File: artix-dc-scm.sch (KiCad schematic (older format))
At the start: 2 parts

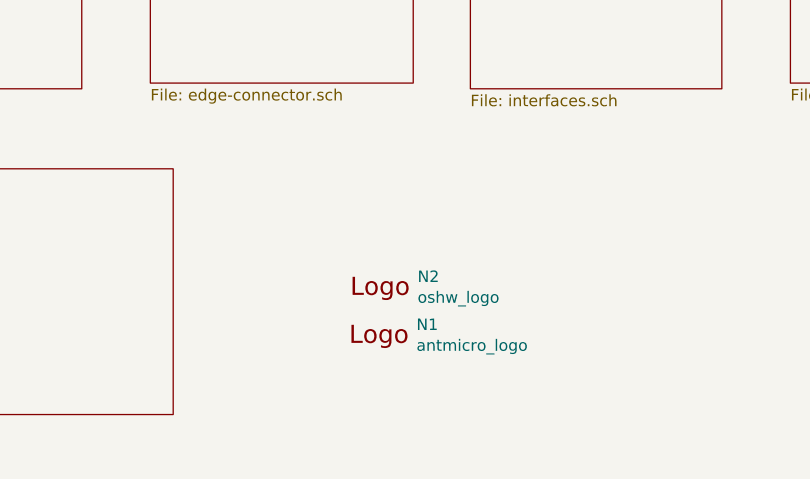
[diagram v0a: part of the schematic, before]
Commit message: Exposed copper and large mounting holes
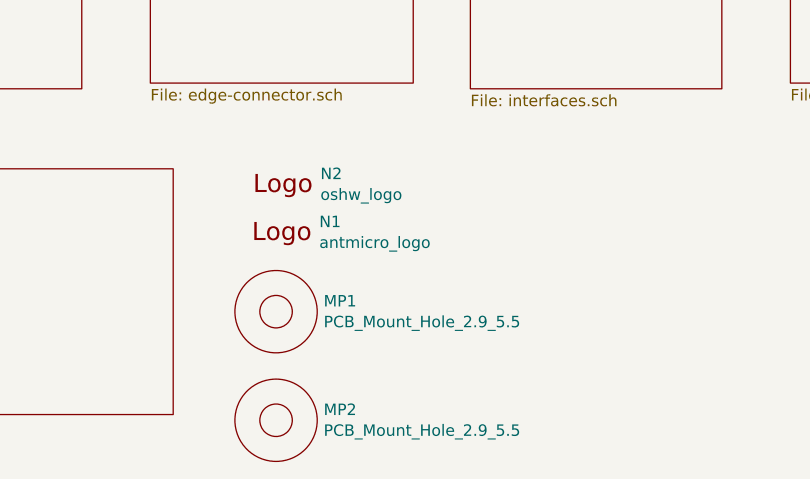
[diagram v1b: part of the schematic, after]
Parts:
- added MP1, MP2: PCB_Mount_Hole_2.9_5.5, artix-dc-scm-footprints:M_2.9_5.5, symbol artix-dc-scm:PCB_Mount_Hole_2.9_5.5
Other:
- moved on the sheet: N1, N2
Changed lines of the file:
@@
 L artix-dc-scm:oshw_logo N2
 U 1 1 6018E5CD
-P 5875 6875
-F 0 "N2" H 6069 6878 50  0000 L CNN
-F 1 "oshw_logo" H 6069 6787 50  0000 L CNN
-F 2 "artix-dc-scm-footprints:oshw-logo" H 5895 6635 50  0001 C CNN
-F 3 "" H 5875 6875 50  0001 C CNN
-	1    5875 6875
+P 5450 6425
+F 0 "N2" H 5644 6428 50  0000 L CNN
+F 1 "oshw_logo" H 5644 6337 50  0000 L CNN
+F 2 "artix-dc-scm-footprints:oshw-logo" H 5470 6185 50  0001 C CNN
+F 3 "" H 5450 6425 50  0001 C CNN
+	1    5450 6425
 	1    0    0    -1
 $EndComp
@@
 L artix-dc-scm:antmicro_logo N1
 U 1 1 6018E8C2
-P 5850 7175
-F 0 "N1" H 6064 7268 50  0000 L CNN
-F 1 "antmicro_logo" H 6064 7177 50  0000 L CNN
-F 2 "artix-dc-scm-footprints:antmicro-logo_scaled_20mm" H 5750 7425 50  0001 C CNN
-F 3 "" H 5850 7525 50  0001 C CNN
-	1    5850 7175
+P 5425 6725
+F 0 "N1" H 5639 6818 50  0000 L CNN
+F 1 "antmicro_logo" H 5639 6727 50  0000 L CNN
+F 2 "artix-dc-scm-footprints:antmicro-logo_scaled_20mm" H 5325 6975 50  0001 C CNN
+F 3 "" H 5425 7075 50  0001 C CNN
+	1    5425 6725
 	1    0    0    -1
 $EndComp
+$Comp
+L artix-dc-scm:PCB_Mount_Hole_2.9_5.5 MP1
+U 1 1 6082760E
+P 5450 7025
+F 0 "MP1" H 5658 7071 50  0000 L CNN
+F 1 "PCB_Mount_Hole_2.9_5.5" H 5658 6980 50  0000 L CNN
+F 2 "artix-dc-scm-footprints:M_2.9_5.5" H 6250 7725 50  0001 C CNN
+F 3 "" H 6400 7825 50  0001 C CNN
+	1    5450 7025
+	1    0    0    -1
+$EndComp
+$Comp
+L artix-dc-scm:PCB_Mount_Hole_2.9_5.5 MP2
+U 1 1 60828DDA
+P 5450 7500
+F 0 "MP2" H 5658 7546 50  0000 L CNN
+F 1 "PCB_Mount_Hole_2.9_5.5" H 5658 7455 50  0000 L CNN
+F 2 "artix-dc-scm-footprints:M_2.9_5.5" H 6250 8200 50  0001 C CNN
+F 3 "" H 6400 8300 50  0001 C CNN
+	1    5450 7500
+	1    0    0    -1
+$EndComp
